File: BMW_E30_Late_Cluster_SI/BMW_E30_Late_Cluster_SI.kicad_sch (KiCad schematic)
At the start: 30 parts, among them J1 SI LED Board, J5 Nexus Connector, Q13 BC337-16, Q19 BC337-25, U1 LP2950-5.0_TO92, Y1 Crystal, Y2 Crystal

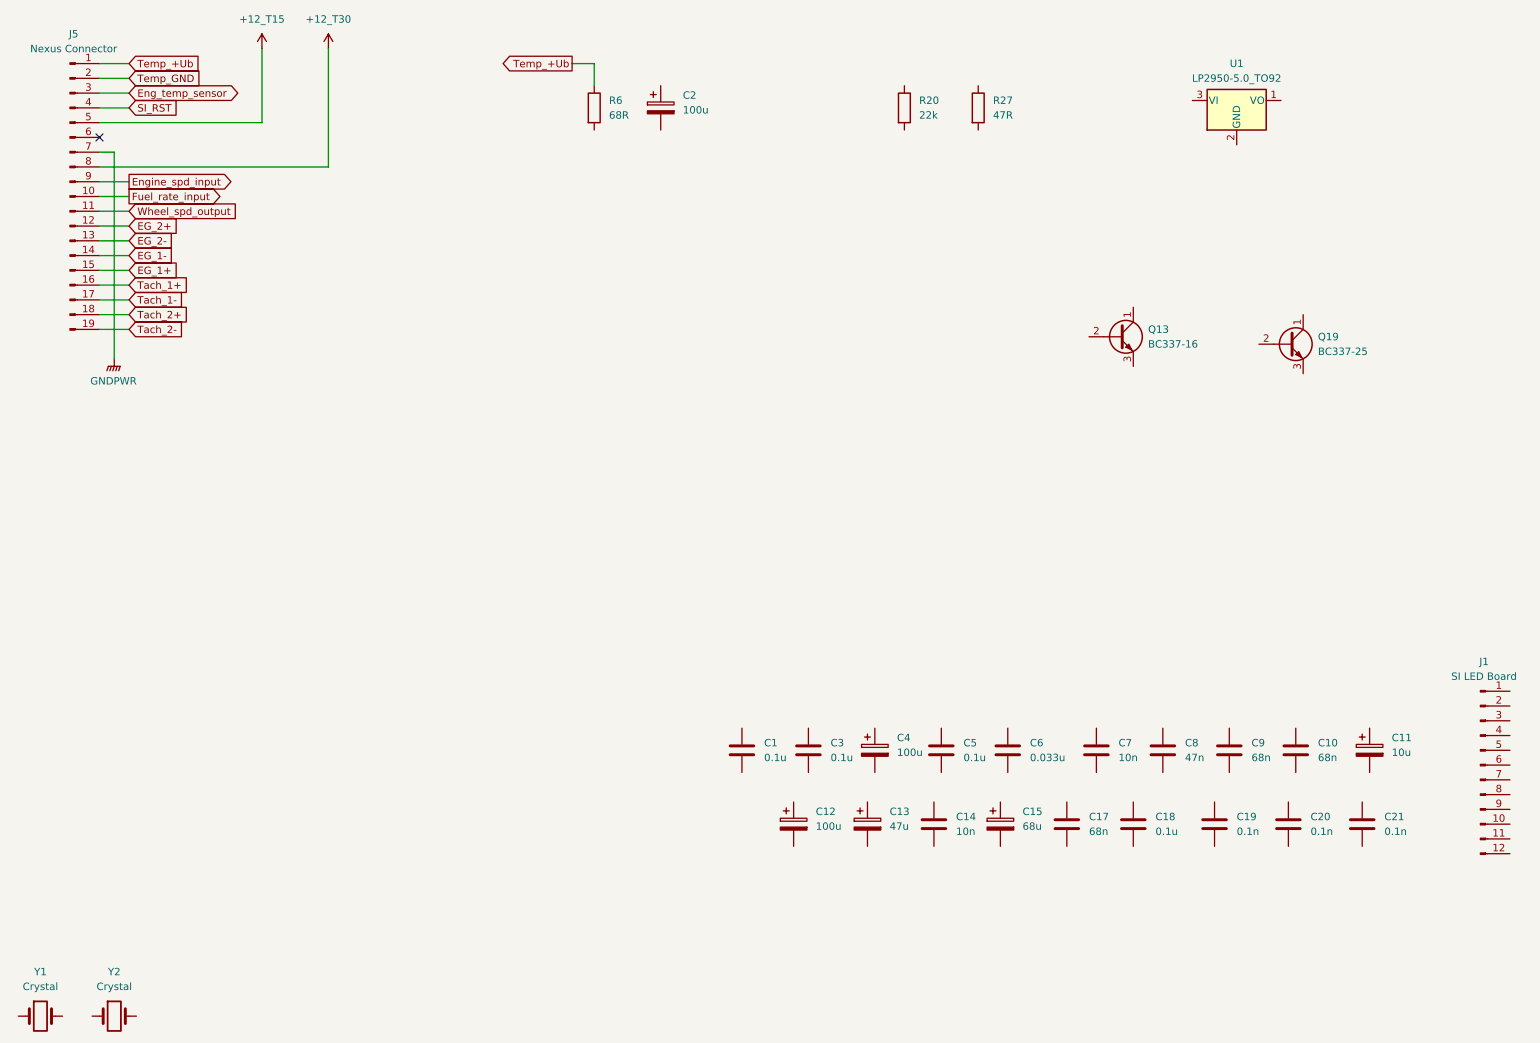
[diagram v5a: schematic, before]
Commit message: Schematic Updates to SI board
Added more resistors and diodes. Only resistors and diodes remain to be entered.
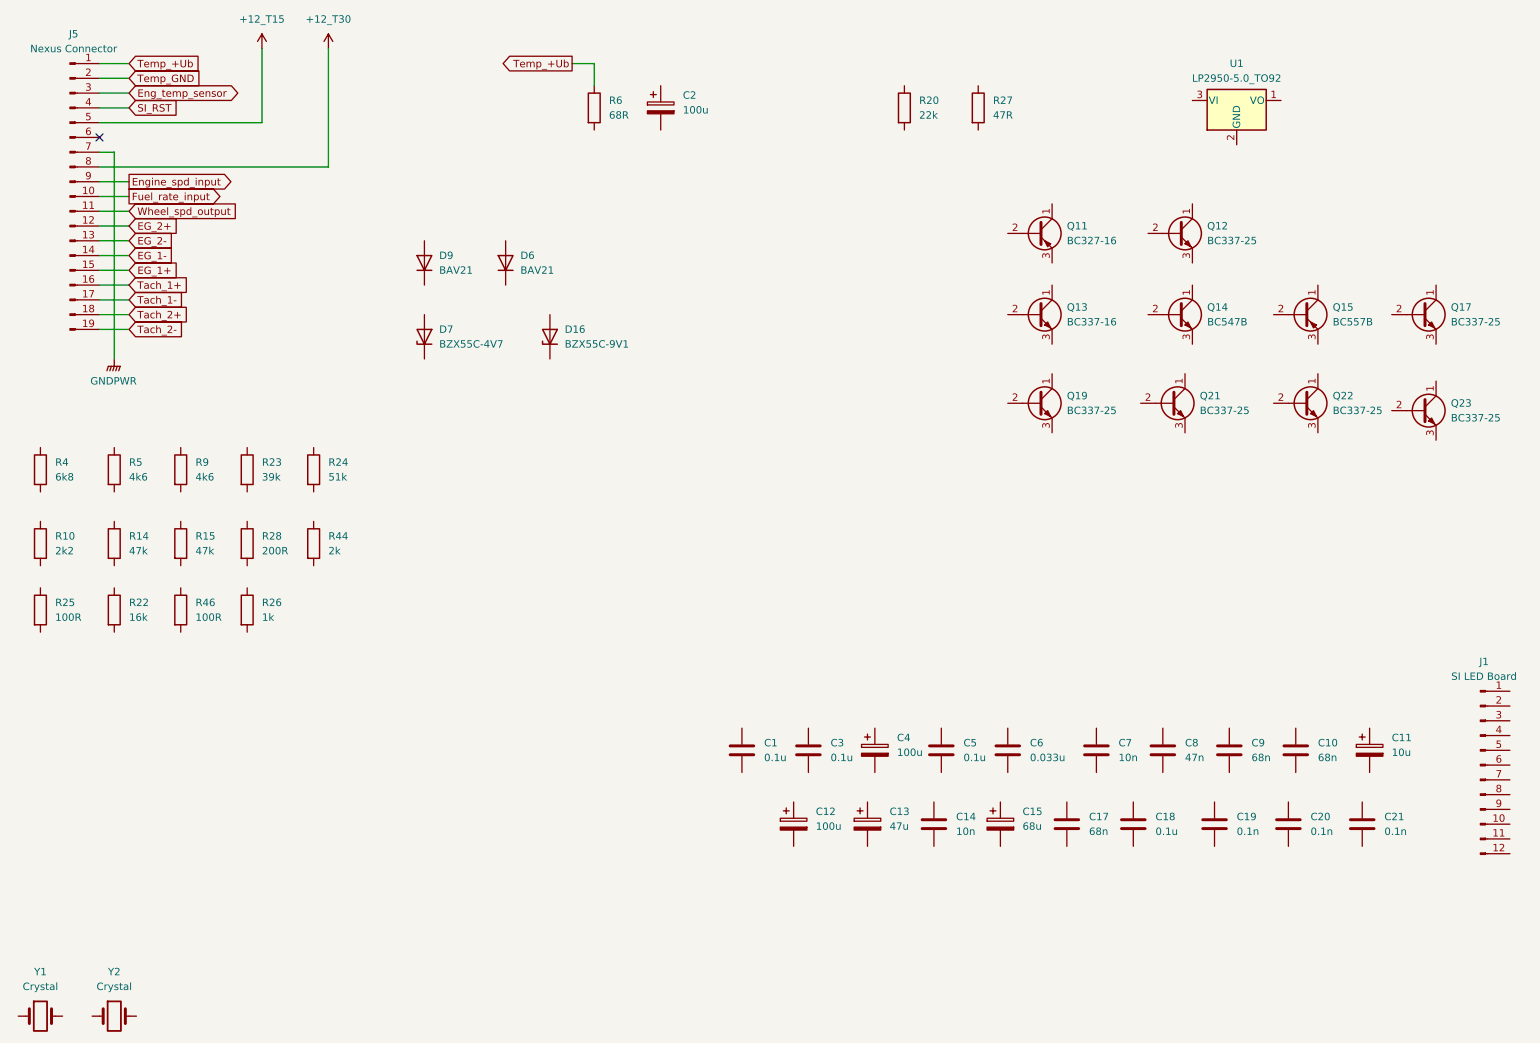
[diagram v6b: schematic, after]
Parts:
- added D16: BZX55C-9V1, symbol Device:D_Zener
- added D6, D9: BAV21, Diode_THT:D_DO-35_SOD27_P7.62mm_Horizontal, symbol Diode:BAV21
- added D7: BZX55C-4V7, symbol Device:D_Zener
- added Q11: BC327-16, Package_TO_SOT_THT:TO-92_Inline_Wide, symbol Transistor_BJT:BC327
- added Q12, Q17, Q21, Q22, Q23: BC337-25, Package_TO_SOT_THT:TO-92_Inline_Wide, symbol Transistor_BJT:BC337
- added Q14: BC547B, Package_TO_SOT_THT:TO-92_Inline_Wide, symbol Transistor_BJT:BC547
- added Q15: BC557B, Package_TO_SOT_THT:TO-92_Inline_Wide, symbol Transistor_BJT:BC557
- added R10: 2k2, SI_THT:R_Axial_Narrow_L6.8mm_D2.4mm_P9.7mm, symbol Device:R
- added R14, R15: 47k, SI_THT:R_Axial_Narrow_L6.8mm_D2.4mm_P9.7mm, symbol Device:R
- added R22: 16k, SI_THT:R_Axial_Narrow_L6.8mm_D2.4mm_P9.7mm, symbol Device:R
- added R23: 39k, SI_THT:R_Axial_Narrow_L6.8mm_D2.4mm_P9.7mm, symbol Device:R
- added R24: 51k, SI_THT:R_Axial_Narrow_L6.8mm_D2.4mm_P9.7mm, symbol Device:R
- added R25, R46: 100R, SI_THT:R_Axial_Narrow_L6.8mm_D2.4mm_P9.7mm, symbol Device:R
- added R26: 1k, SI_THT:R_Axial_Narrow_L6.8mm_D2.4mm_P9.7mm, symbol Device:R
- added R28: 200R, SI_THT:R_Axial_Narrow_L6.8mm_D2.4mm_P9.7mm, symbol Device:R
- added R4: 6k8, SI_THT:R_Axial_Narrow_L6.8mm_D2.4mm_P9.7mm, symbol Device:R
- added R44: 2k, SI_THT:R_Axial_Narrow_L6.8mm_D2.4mm_P9.7mm, symbol Device:R
- added R5, R9: 4k6, SI_THT:R_Axial_Narrow_L6.8mm_D2.4mm_P9.7mm, symbol Device:R
- Q13, Q19: footprint Package_TO_SOT_THT:TO-92_Inline -> Package_TO_SOT_THT:TO-92_Inline_Wide
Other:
- moved on the sheet: Q13, Q19

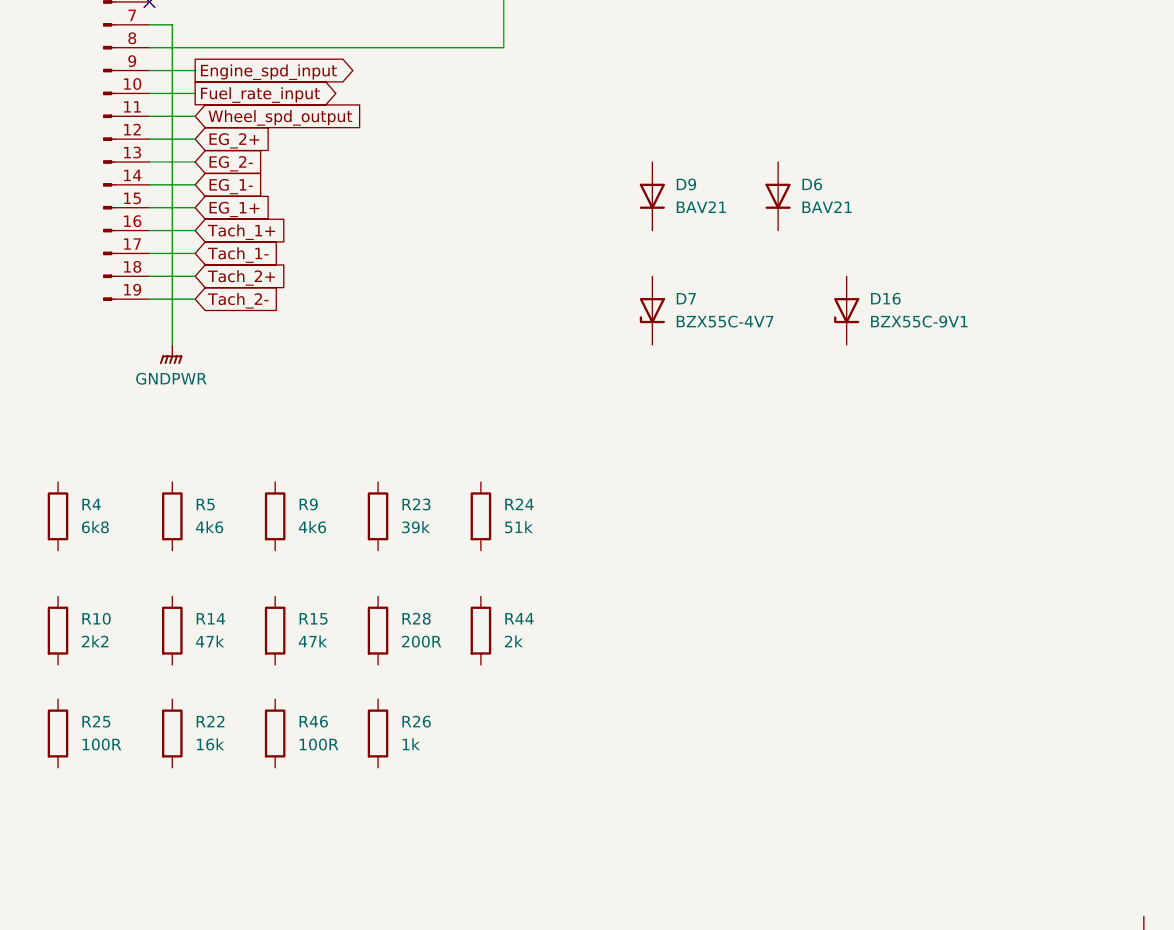
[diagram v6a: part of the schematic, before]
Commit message: updates to SI schematic
Added several more resistors and diodes to the SI schematic.
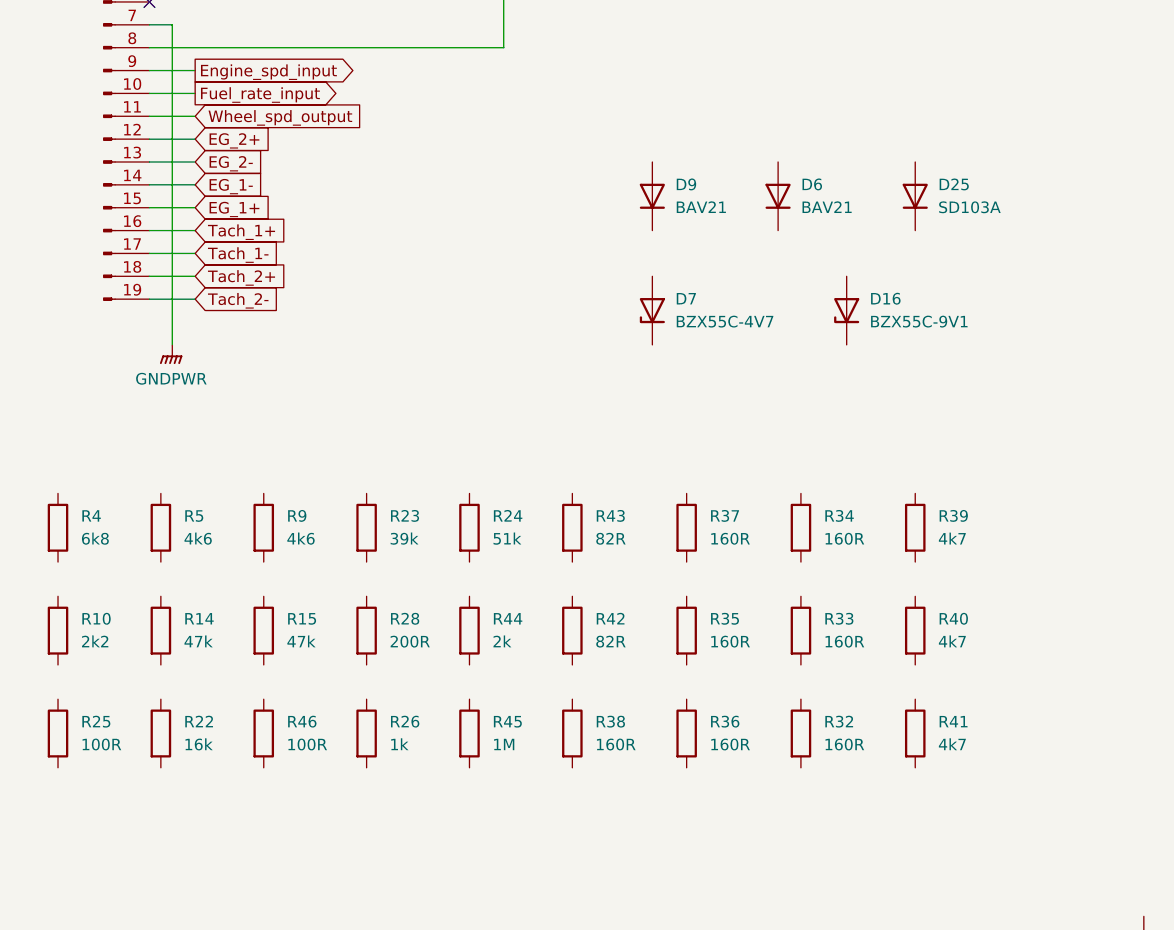
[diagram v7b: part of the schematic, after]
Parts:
- added D25: SD103A, symbol Device:D
- added R32, R33, R34, R35, R36, R37, R38: 160R, SI_THT:R_Axial_Narrow_L6.8mm_D2.4mm_P9.7mm, symbol Device:R
- added R39, R40, R41: 4k7, SI_THT:R_Axial_Narrow_L6.8mm_D2.4mm_P9.7mm, symbol Device:R
- added R42, R43: 82R, SI_THT:R_Axial_Narrow_L6.8mm_D2.4mm_P9.7mm, symbol Device:R
- added R45: 1M, SI_THT:R_Axial_Narrow_L6.8mm_D2.4mm_P9.7mm, symbol Device:R
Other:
- moved on the sheet: R14, R15, R22, R23, R24, R26, R28, R4, R44, R46, R5, R9

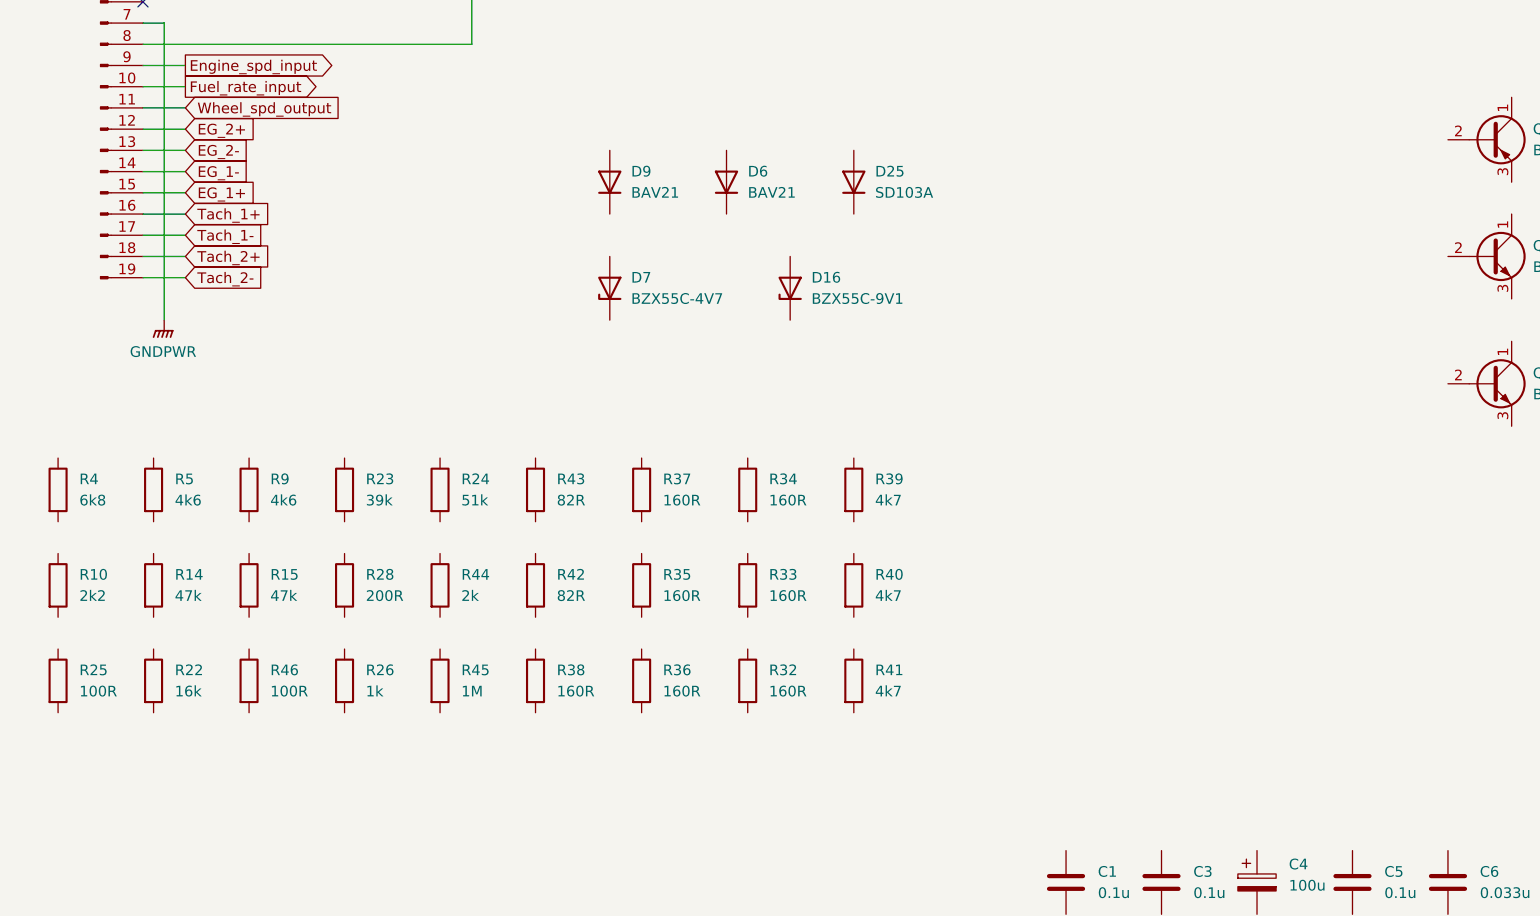
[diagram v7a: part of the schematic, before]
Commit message: Update SI Schematic
Added all of the components except for the 4 IC's. Those will require custom footprints as the chips are NLA with no datasheets.
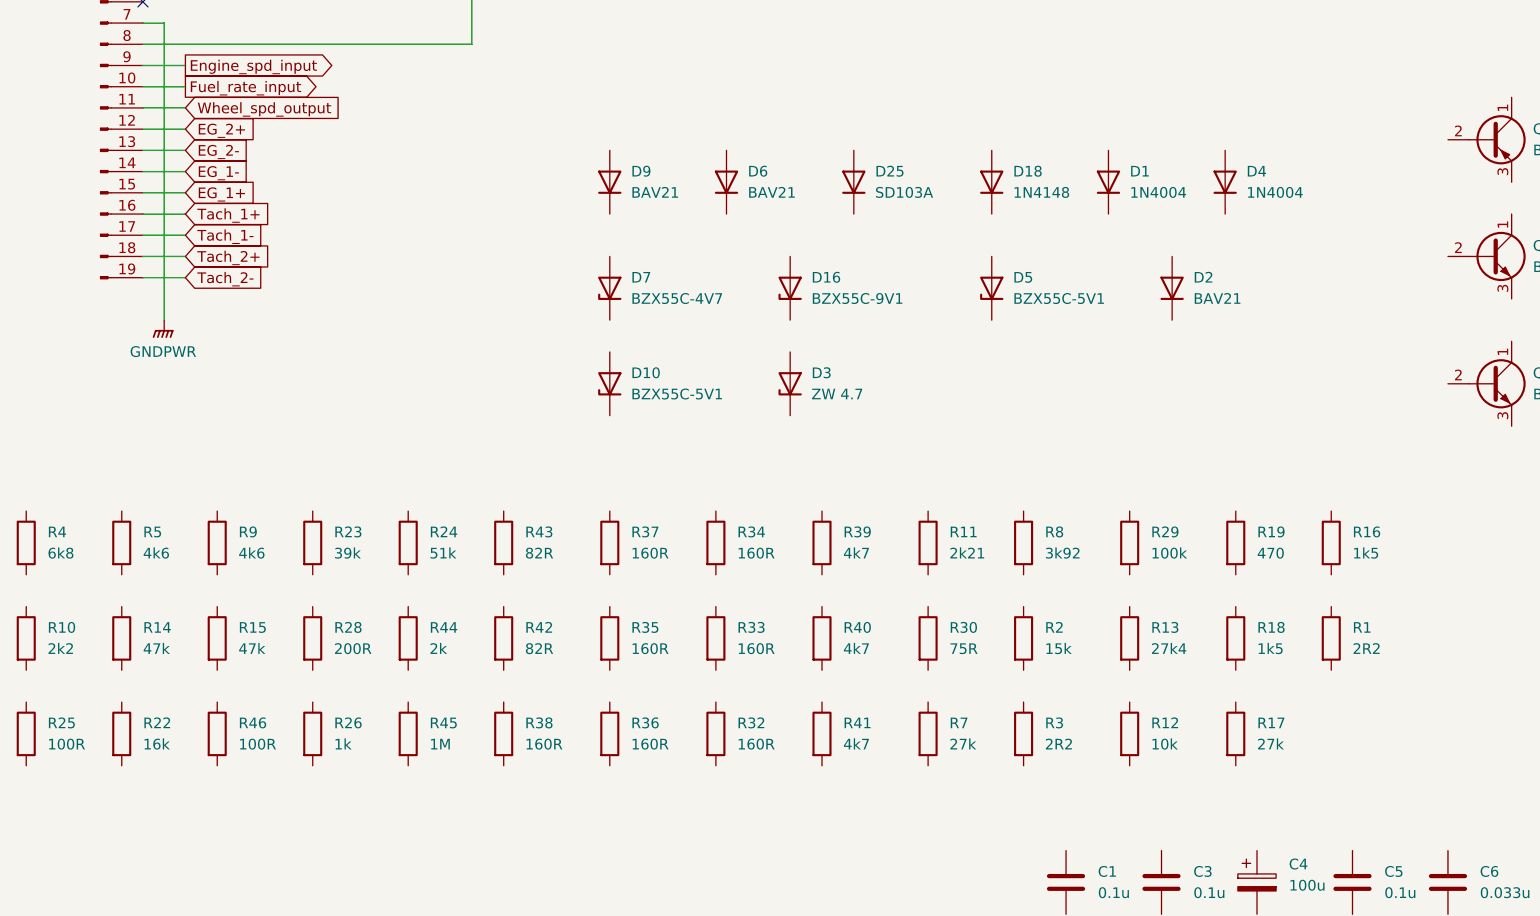
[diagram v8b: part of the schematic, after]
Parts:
- added D1, D4: 1N4004, Diode_THT:D_DO-41_SOD81_P10.16mm_Horizontal, symbol Diode:1N4004
- added D10, D5: BZX55C-5V1, symbol Device:D_Zener
- added D18: 1N4148, symbol Device:D
- added D2: BAV21, Diode_THT:D_DO-35_SOD27_P7.62mm_Horizontal, symbol Diode:BAV21
- added D3: ZW 4.7, symbol Device:D_Zener
- added R1, R3: 2R2, SI_THT:R_Axial_Narrow_L6.8mm_D2.4mm_P9.7mm, symbol Device:R
- added R11: 2k21, SI_THT:R_Axial_Narrow_L6.8mm_D2.4mm_P9.7mm, symbol Device:R
- added R12: 10k, SI_THT:R_Axial_Narrow_L6.8mm_D2.4mm_P9.7mm, symbol Device:R
- added R13: 27k4, SI_THT:R_Axial_Narrow_L6.8mm_D2.4mm_P9.7mm, symbol Device:R
- added R16, R18: 1k5, SI_THT:R_Axial_Narrow_L6.8mm_D2.4mm_P9.7mm, symbol Device:R
- added R17, R7: 27k, SI_THT:R_Axial_Narrow_L6.8mm_D2.4mm_P9.7mm, symbol Device:R
- added R19: 470, SI_THT:R_Axial_Narrow_L6.8mm_D2.4mm_P9.7mm, symbol Device:R
- added R2: 15k, SI_THT:R_Axial_Narrow_L6.8mm_D2.4mm_P9.7mm, symbol Device:R
- added R29: 100k, SI_THT:R_Axial_Narrow_L6.8mm_D2.4mm_P9.7mm, symbol Device:R
- added R30: 75R, SI_THT:R_Axial_Narrow_L6.8mm_D2.4mm_P9.7mm, symbol Device:R
- added R8: 3k92, SI_THT:R_Axial_Narrow_L6.8mm_D2.4mm_P9.7mm, symbol Device:R
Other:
- moved on the sheet: R10, R14, R15, R22, R23, R24, R25, R26, R28, R32, R33, R34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
